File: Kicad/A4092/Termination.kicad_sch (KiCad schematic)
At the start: 30 parts, among them J1 5749721-7, J2 5749721-7, J3 TO-LED, J4 TO-MB, J5 TO-A3000-LED, J6 TO-A3000-MB, U10 DS21S07A, U11 DS21S07A, U12 DS21S07A

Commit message: Clean up pull-up resistors
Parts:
- removed R1: 4K7, Resistor_SMD:R_0603_1608Metric_Pad0.98x0.95mm_HandSolder, symbol Device:R_Small
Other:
- title: A4092 -> Cheetah UW
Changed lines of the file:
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@@
 	(paper "A4")
 	(title_block
-		(title "A4092")
-		(rev "PROTO0")
+		(title "Cheetah UW")
+		(rev "PROTO1")
 		(company "amiga.technology")
 	)
@@
 		)
 	)
-	(global_label "PLD_EXT_TERM"
-		(shape input)
-		(at 57.15 153.67 0)
-		(fields_autoplaced yes)
-		(effects
-			(font
-				(size 1.27 1.27)
-			)
-			(justify left)
-		)
-		(property "Intersheetrefs" "${INTERSHEET_REFS}"
-			(at 73.8026 153.67 0)
-			(effects
-				(font
-					(size 1.27 1.27)
-				)
-				(justify left)
-				(hide yes)
-			)
-		)
-	)
 	(global_label "GND"
 		(shape input)
@@
 		)
 	)
-	(global_label "V5"
-		(shape input)
-		(at 52.07 153.67 180)
-		(fields_autoplaced yes)
-		(effects
-			(font
-				(size 1.27 1.27)
-			)
-			(justify right)
-		)
-		(property "Intersheetrefs" "${INTERSHEET_REFS}"
-			(at 46.7867 153.67 0)
-			(effects
-				(font
-					(size 1.27 1.27)
-				)
-				(justify right)
-				(hide yes)
-			)
-		)
-	)
 	(global_label "GND"
 		(shape input)
@@
 					(unit 1)
 				)
-			)
-		)
-	)
-	(symbol
-		(lib_id "Device:R_Small")
-		(at 54.61 153.67 270)
-		(unit 1)
-		(exclude_from_sim no)
-		(in_bom yes)
-		(on_board yes)
-		(dnp no)
-		(property "Reference" "R1"
-			(at 54.61 155.702 90)
-			(effects
-				(font
-					(size 1.016 1.016)
-				)
-			)
-		)
-		(property "Value" "4K7"
-			(at 54.61 153.67 90)
-			(effects
-				(font
-					(size 1.016 1.016)
-				)
-			)
-		)
-		(property "Footprint" "Resistor_SMD:R_0603_1608Metric_Pad0.98x0.95mm_HandSolder"
-			(at 54.61 153.67 0)
-			(effects
-				(font
-					(size 1.27 1.27)
-				)
-				(hide yes)
-			)
-		)
-		(property "Datasheet" "~"
-			(at 54.61 153.67 0)
-			(effects
-				(font
-					(size 1.27 1.27)
-				)
-				(hide yes)
-			)
-		)
-		(property "Description" "Resistor, small symbol"
-			(at 54.61 153.67 0)
-			(effects
-				(font
-					(size 1.27 1.27)
-				)
-				(hide yes)
-			)
-		)
-		(property "LCSC Part #" "C23162"
-			(at 54.61 153.67 90)
-			(effects
-				(font
-					(size 1.27 1.27)
-				)
-				(hide yes)
-			)
-		)
-		(pin "2"
-		)
-		(pin "1"
-		)
-		(instances
-			(project "A4092"
-				(path "/8f9f4021-47aa-41d9-bea7-f6ccf72098bb/53e9e23b-3b92-4a87-a15c-9c224d6145c5"
-					(reference "R1")
-					(unit 1)
-				)

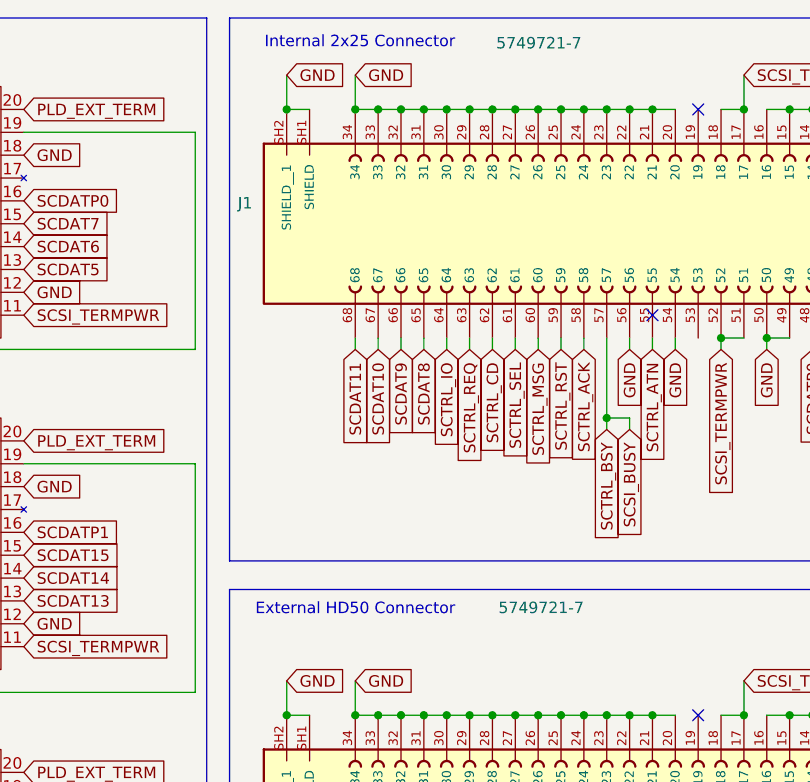
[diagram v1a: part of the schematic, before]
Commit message: Fix description and part numbers for SCSI connectors
Was still using the description for SCSI-2
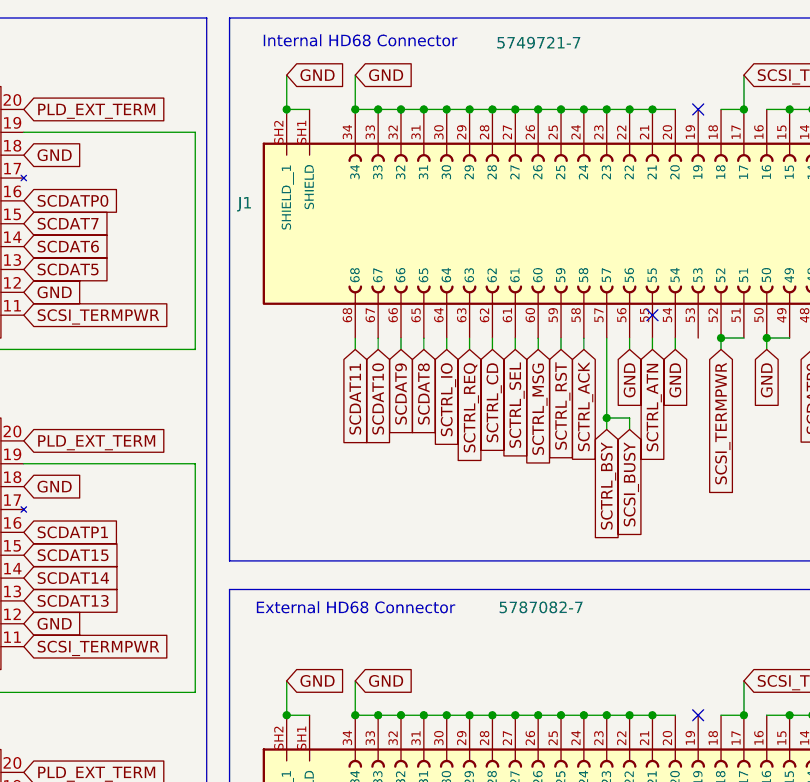
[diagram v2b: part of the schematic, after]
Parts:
- J1: LCSC Part # (none) -> C591675
- J2: value 5749721-7 -> 5787082-7; LCSC Part # (none) -> C591676
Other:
- note added: "External HD68 Connector"
- note added: "Internal HD68 Connector"
- note removed: "External HD50 Connector"
- note removed: "Internal 2x25 Connector"
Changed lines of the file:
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@@
 		)
 	)
-	(text "Internal 2x25 Connector"
+	(text "Internal HD68 Connector"
 		(exclude_from_sim no)
 		(at 98.298 18.034 0)
@@
 		)
 	)
-	(text "External HD50 Connector"
+	(text "External HD68 Connector"
 		(exclude_from_sim no)
 		(at 97.79 81.026 0)
@@
 			)
 		)
-		(property "Value" "5749721-7"
+		(property "Value" "5787082-7"
 			(at 123.19 80.772 90)
 			(effects
@@
 			)
 		)
+		(property "LCSC Part #" "C591676"
+			(at 135.89 105.41 90)
+			(effects
+				(font
+					(size 1.27 1.27)
+				)
+				(hide yes)
+			)
+		)
 		(pin "26"
 		)
@@
 				(hide yes)
 			)
+		)
+		(property "LCSC Part #" "C591675"
+			(at 135.89 38.1 90)
+			(effects
+				(font
+					(size 1.27 1.27)
+				)
+				(hide yes)
+			)

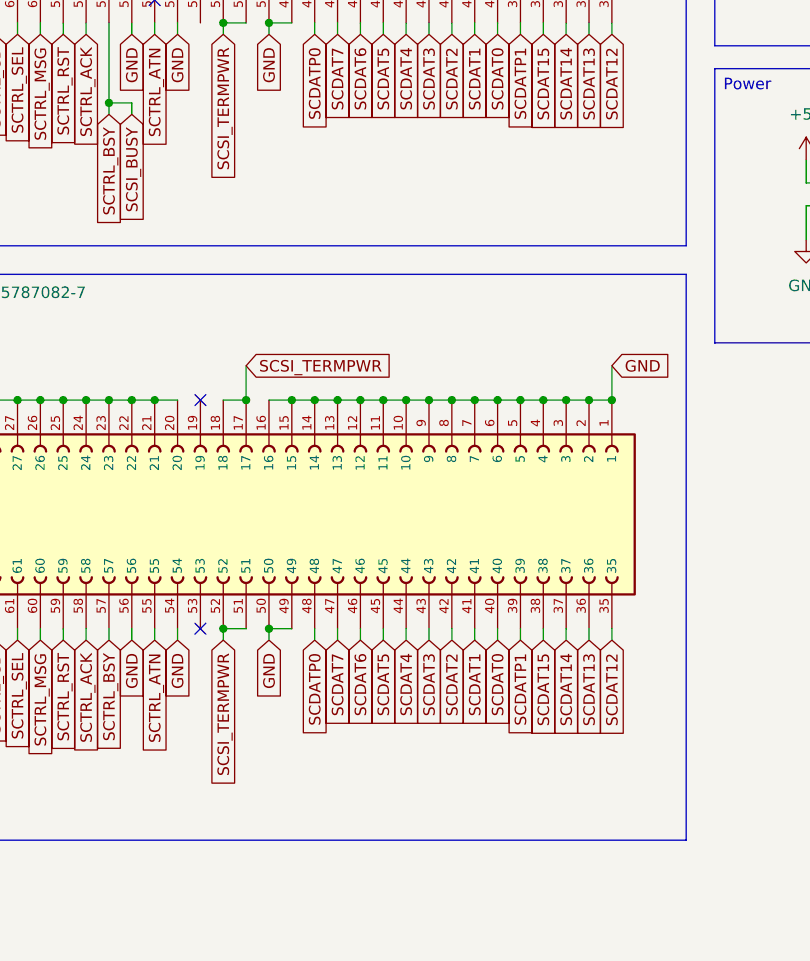
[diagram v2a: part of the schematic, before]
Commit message: Rehaul clock circuit in schematics
and try to add most of the LCSC part numbers
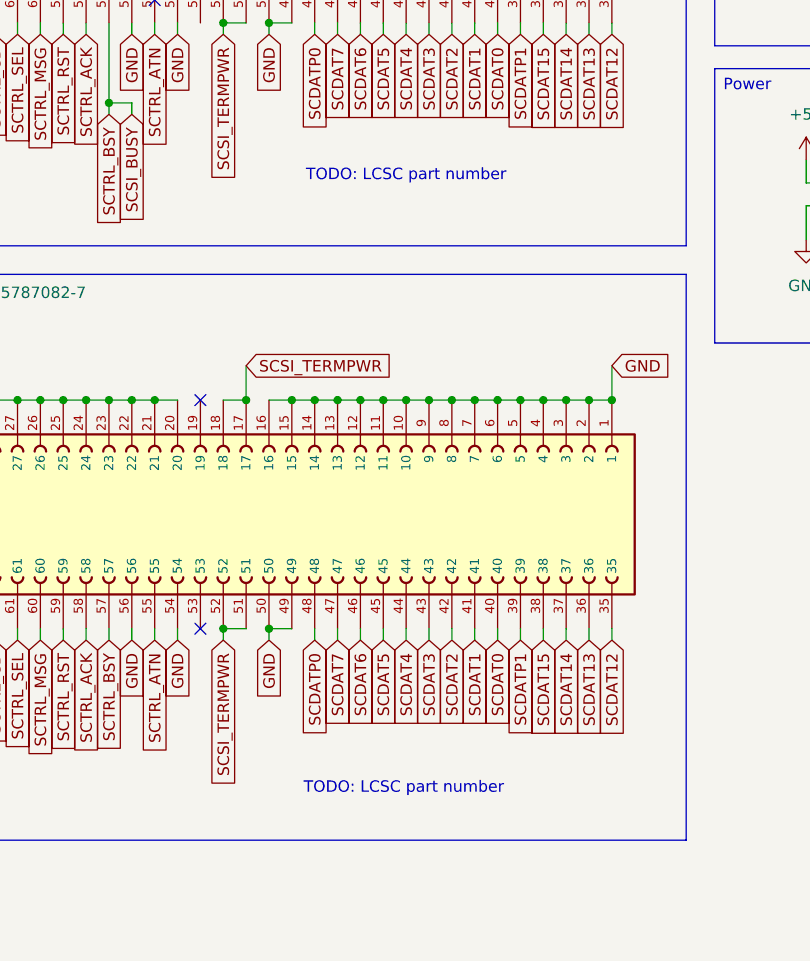
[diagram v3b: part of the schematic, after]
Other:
- note added: "TODO: LCSC part number"
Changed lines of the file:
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@@
+		)
+	)
+	(text "TODO: LCSC part number"
+		(exclude_from_sim no)
+		(at 158.496 135.89 0)
+		(effects
+			(font
+				(size 1.27 1.27)
+			)
 		)
 	)
@@
 		(effects
 			(font
+				(size 1.27 1.27)
+			)
+		)
+	)
+	(text "TODO: LCSC part number"
+		(exclude_from_sim no)
+		(at 158.75 67.818 0)
+		(effects
+			(font
